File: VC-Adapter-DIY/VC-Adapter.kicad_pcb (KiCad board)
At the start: 2 copper layers, 40 x 26.8 mm, 4 parts, among them J1 gba_linkport, U1 XIAO_ESP32_S3, U2 BOB-12009

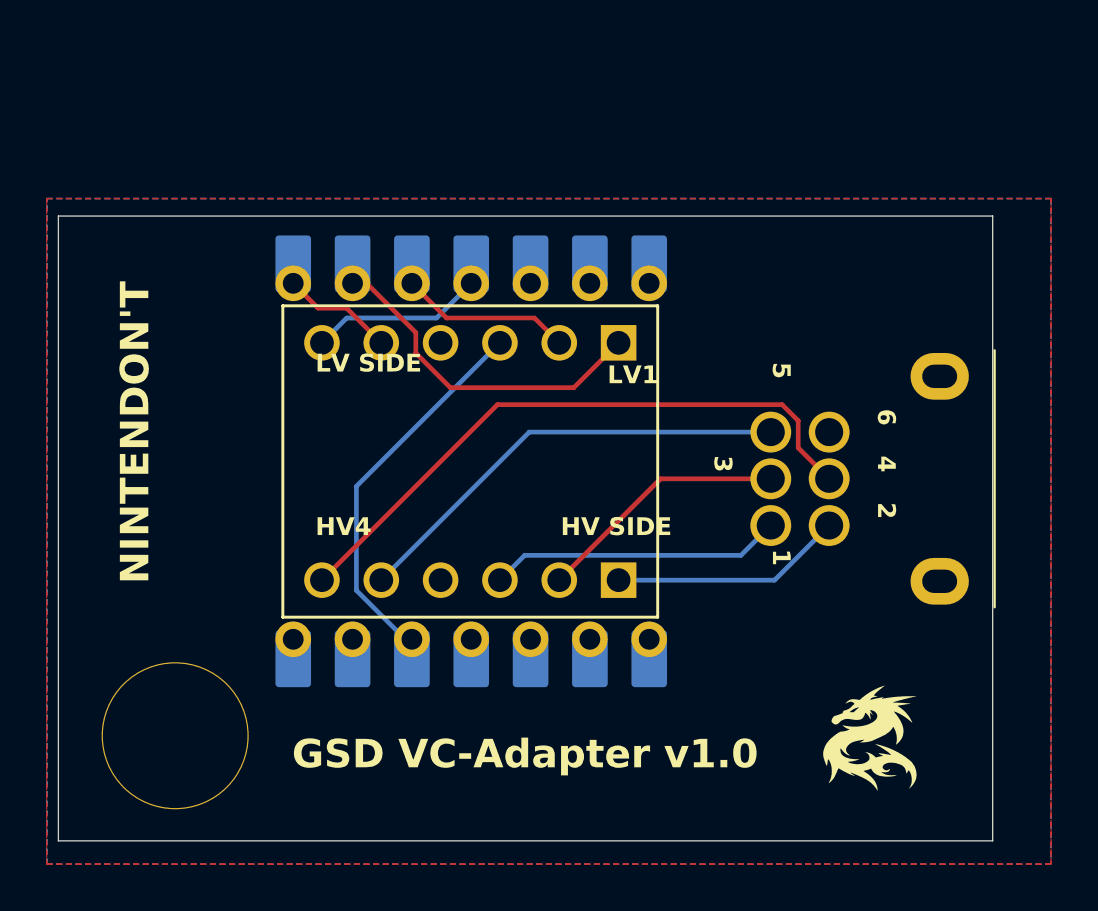
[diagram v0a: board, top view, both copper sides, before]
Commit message: Added voltage divider and battery EN support
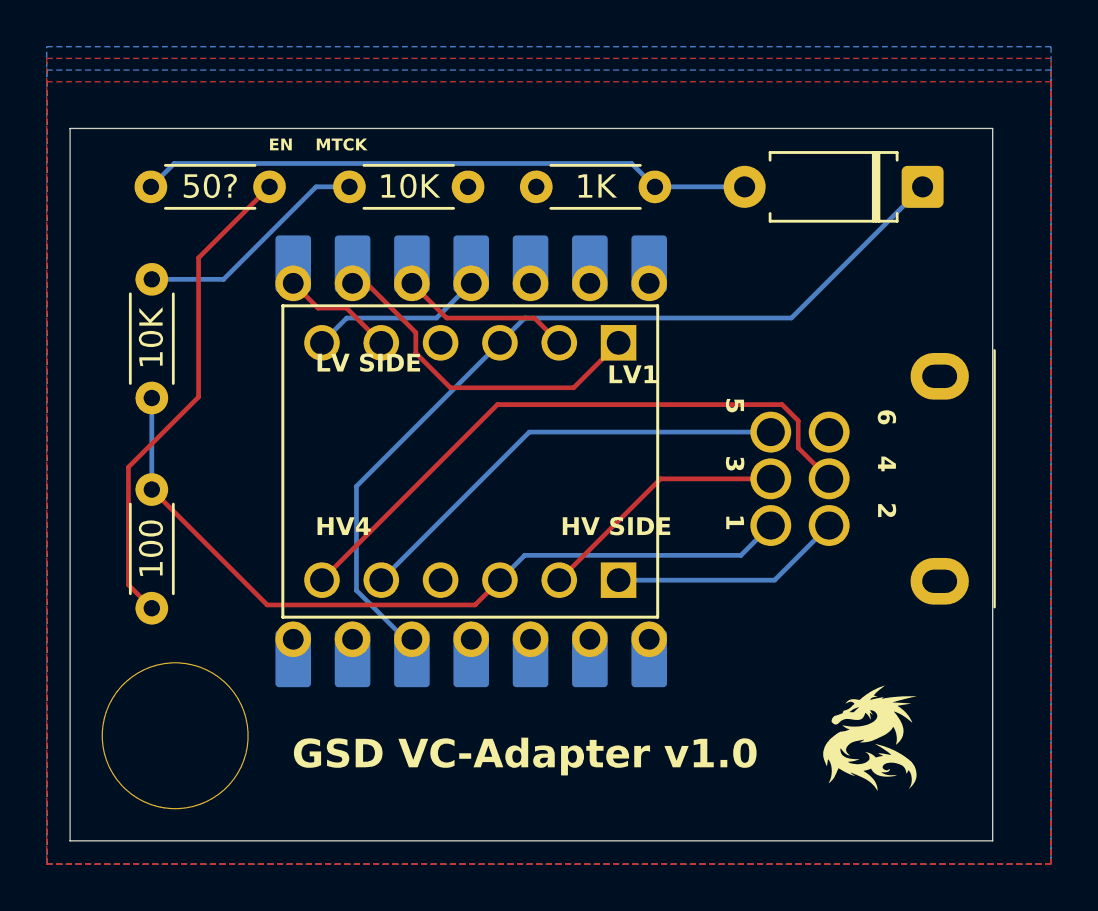
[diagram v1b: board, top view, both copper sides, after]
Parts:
- added 100: 100, Resistor_THT:R_Axial_DIN0204_L3.6mm_D1.6mm_P5.08mm_Horizontal, F.Cu at (123.5, 101.5)
- added 10K: 10K, Resistor_THT:R_Axial_DIN0204_L3.6mm_D1.6mm_P5.08mm_Horizontal, F.Cu at (132.0, 88.5)
- added 10K: 10K, Resistor_THT:R_Axial_DIN0204_L3.6mm_D1.6mm_P5.08mm_Horizontal, F.Cu at (123.5, 97.5)
- added 1K: 1k, Resistor_THT:R_Axial_DIN0204_L3.6mm_D1.6mm_P5.08mm_Horizontal, F.Cu at (145.0, 88.5)
- added 50?: 50?, Resistor_THT:R_Axial_DIN0204_L3.6mm_D1.6mm_P5.08mm_Horizontal, F.Cu at (128.5, 88.5)
- added D1: D, Diode_THT:D_A-405_P7.62mm_Horizontal, F.Cu at (156.5, 88.5)
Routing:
- net Net-(D1-A): track 0.00 -> 26.2 mm
- net Net-(J1-Pin_1): track 12.6 -> 33.9 mm
- net Net-(R4-Pad2): track 0.00 -> 21.0 mm
- net Net-(D1-K): track 16.4 -> 37.2 mm
- net Net-(R1-Pad2): track 0.00 -> 10.1 mm
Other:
- board size 40 x 26.8 mm -> 39.5 x 30.5 mm
- board text added: "EN"
- board text added: "MTCK"
- board text removed: "NINTENDON'T"
